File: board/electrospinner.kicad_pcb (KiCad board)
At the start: 2 copper layers, 40 parts, among them J1 12Vin, J2 Programmer, J3 MotorConnector, J4 TempSensor, J5 USB_B, SW1 ResetBTN, U1 TPS62147, U2 FT230XS, U3 MSP430G2553IPW20

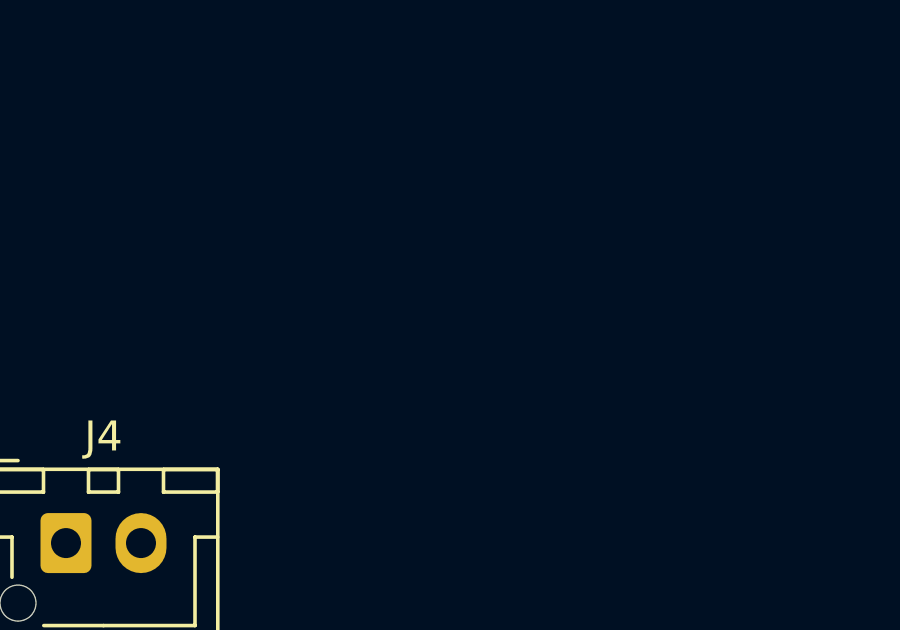
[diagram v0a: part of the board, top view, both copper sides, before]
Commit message: Updates schematic for rev6
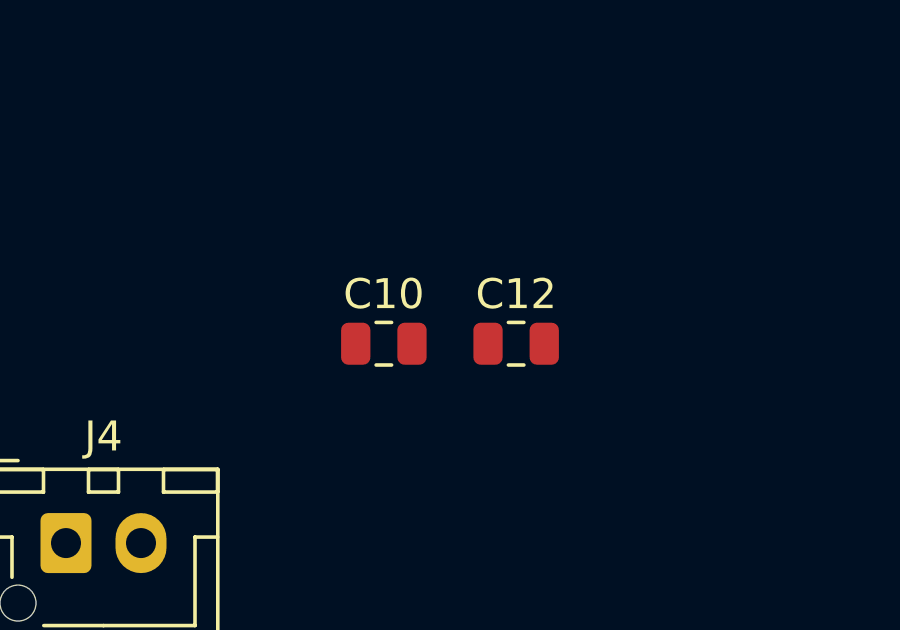
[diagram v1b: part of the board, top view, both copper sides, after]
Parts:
- added C10: 10uF, Capacitor_SMD:C_0805_2012Metric, F.Cu at (175.7, 68.3)
- added C12: 22uF, Capacitor_SMD:C_0805_2012Metric, F.Cu at (180.1, 68.3)
- J4: value TempSensor -> TempSensorConnector
- L1: value 1uH -> 2.2uH
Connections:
- R4 pad 1: /~RST -> +3V3
- R4 pad 2: GNDD -> /~RST
- SW1 pad 1: /~RST -> GNDD
- SW1 pad 2: +3V3 -> /~RST
- U1 pad 11: +12V -> GNDD
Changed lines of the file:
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@@
     (tracks 0)
     (zones 0)
-    (modules 40)
+    (modules 42)
     (nets 31)
   )
@@
     )
     (pad 11 smd rect (at -0.749998 -1.4) (size 0.249999 0.599999) (layers F.Paste)
-      (net 14 +12V))
+      (net 1 GNDD))
     (pad 11 smd rect (at -0.749998 -1.4) (size 0.249999 0.599999) (layers F.Mask)
-      (net 14 +12V))
+      (net 1 GNDD))
     (pad 11 smd rect (at -0.749998 -1.4) (size 0.249999 0.599999) (layers F.Cu)
-      (net 14 +12V))
+      (net 1 GNDD))
     (pad 10 smd rect (at -0.25 -1.4) (size 0.249999 0.599999) (layers F.Paste)
       (net 1 GNDD))
@@
     )
     (pad 1 thru_hole circle (at 6.5 0 90) (size 2 2) (drill 1.1) (layers *.Cu *.Mask)
+      (net 1 GNDD))
+    (pad 2 thru_hole circle (at 6.5 4.5 90) (size 2 2) (drill 1.1) (layers *.Cu *.Mask)
       (net 19 /~RST))
-    (pad 2 thru_hole circle (at 6.5 4.5 90) (size 2 2) (drill 1.1) (layers *.Cu *.Mask)
-      (net 17 +3V3))
     (pad 1 thru_hole circle (at 0 0 90) (size 2 2) (drill 1.1) (layers *.Cu *.Mask)
+      (net 1 GNDD))
+    (pad 2 thru_hole circle (at 0 4.5 90) (size 2 2) (drill 1.1) (layers *.Cu *.Mask)
       (net 19 /~RST))
-    (pad 2 thru_hole circle (at 0 4.5 90) (size 2 2) (drill 1.1) (layers *.Cu *.Mask)
-      (net 17 +3V3))
     (model ${KISYS3DMOD}/Button_Switch_THT.3dshapes/SW_PUSH_6mm_H5mm.wrl
       (at (xyz 0 0 0))
@@
     (fp_line (start -1 0.6) (end -1 -0.6) (layer F.Fab) (width 0.1))
     (pad 2 smd roundrect (at 0.9375 0) (size 0.975 1.4) (layers F.Cu F.Paste F.Mask) (roundrect_rratio 0.25)
-      (net 1 GNDD))
+      (net 19 /~RST))
     (pad 1 smd roundrect (at -0.9375 0) (size 0.975 1.4) (layers F.Cu F.Paste F.Mask) (roundrect_rratio 0.25)
-      (net 19 /~RST))
+      (net 17 +3V3))
     (model ${KISYS3DMOD}/Resistor_SMD.3dshapes/R_0805_2012Metric.wrl
       (at (xyz 0 0 0))
@@
       (effects (font (size 1 1) (thickness 0.15)))
     )
-    (fp_text value 1uH (at 0 1.65 270) (layer F.Fab)
+    (fp_text value 2.2uH (at 0 1.65 270) (layer F.Fab)
       (effects (font (size 1 1) (thickness 0.15)))
     )
@@
       (effects (font (size 1 1) (thickness 0.15)))
     )
-    (fp_text value TempSensor (at 1.25 4.6) (layer F.Fab)
+    (fp_text value TempSensorConnector (at 1.25 4.6) (layer F.Fab)
       (effects (font (size 1 1) (thickness 0.15)))
     )
@@
       (at (xyz 0 0 0))
       (scale (xyz 1 1 1))
+      (rotate (xyz 0 0 0))
+    )
+  )
+  (module Capacitor_SMD:C_0805_2012Metric (layer F.Cu)
+    (at 175.695001 68.285001)
+    (descr "Capacitor SMD 0805 (2012 Metric), square (rectangular) end terminal, IPC_7351 nominal, (Body size source: https://docs.google.com/spreadsheets/d/1BsfQQcO9C6DZCsRaXUlFlo91Tg2WpOkGARC1WS5S8t0/edit?usp=sharing), generated with kicad-footprint-generator")
+    (tags capacitor)
+    (attr smd)
+    (fp_text reference C10 (at 0 -1.65) (layer F.SilkS)
+      (effects (font (size 1 1) (thickness 0.15)))
+    )
+    (fp_text value 10uF (at 0 1.65) (layer F.Fab)
+      (effects (font (size 1 1) (thickness 0.15)))
+    )
+    (fp_text user %R (at 0 0) (layer F.Fab)
+      (effects (font (size 0.5 0.5) (thickness 0.08)))
+    )
+    (fp_line (start 1.68 0.95) (end -1.68 0.95) (layer F.CrtYd) (width 0.05))
+    (fp_line (start 1.68 -0.95) (end 1.68 0.95) (layer F.CrtYd) (width 0.05))
+    (fp_line (start -1.68 -0.95) (end 1.68 -0.95) (layer F.CrtYd) (width 0.05))
+    (fp_line (start -1.68 0.95) (end -1.68 -0.95) (layer F.CrtYd) (width 0.05))
+    (fp_line (start -0.258578 0.71) (end 0.258578 0.71) (layer F.SilkS) (width 0.12))
+    (fp_line (start -0.258578 -0.71) (end 0.258578 -0.71) (layer F.SilkS) (width 0.12))
+    (fp_line (start 1 0.6) (end -1 0.6) (layer F.Fab) (width 0.1))
+    (fp_line (start 1 -0.6) (end 1 0.6) (layer F.Fab) (width 0.1))
+    (fp_line (start -1 -0.6) (end 1 -0.6) (layer F.Fab) (width 0.1))
+    (fp_line (start -1 0.6) (end -1 -0.6) (layer F.Fab) (width 0.1))
+    (pad 2 smd roundrect (at 0.9375 0) (size 0.975 1.4) (layers F.Cu F.Paste F.Mask) (roundrect_rratio 0.25)
+      (net 1 GNDD))
+    (pad 1 smd roundrect (at -0.9375 0) (size 0.975 1.4) (layers F.Cu F.Paste F.Mask) (roundrect_rratio 0.25)
+      (net 17 +3V3))
+    (model ${KISYS3DMOD}/Capacitor_SMD.3dshapes/C_0805_2012Metric.wrl
+      (at (xyz 0 0 0))
+      (scale (xyz 1 1 1))
+      (rotate (xyz 0 0 0))
+    )
+  )
+  (module Capacitor_SMD:C_0805_2012Metric (layer F.Cu)
+    (at 180.105001 68.285001)
+    (descr "Capacitor SMD 0805 (2012 Metric), square (rectangular) end terminal, IPC_7351 nominal, (Body size source: https://docs.google.com/spreadsheets/d/1BsfQQcO9C6DZCsRaXUlFlo91Tg2WpOkGARC1WS5S8t0/edit?usp=sharing), generated with kicad-footprint-generator")
+    (tags capacitor)
+    (attr smd)
+    (fp_text reference C12 (at 0 -1.65) (layer F.SilkS)
+      (effects (font (size 1 1) (thickness 0.15)))
+    )
+    (fp_text value 22uF (at 0 1.65) (layer F.Fab)
+      (effects (font (size 1 1) (thickness 0.15)))
+    )
+    (fp_line (start -1 0.6) (end -1 -0.6) (layer F.Fab) (width 0.1))
+    (fp_line (start -1 -0.6) (end 1 -0.6) (layer F.Fab) (width 0.1))
+    (fp_line (start 1 -0.6) (end 1 0.6) (layer F.Fab) (width 0.1))
+    (fp_line (start 1 0.6) (end -1 0.6) (layer F.Fab) (width 0.1))
+    (fp_line (start -0.258578 -0.71) (end 0.258578 -0.71) (layer F.SilkS) (width 0.12))
+    (fp_line (start -0.258578 0.71) (end 0.258578 0.71) (layer F.SilkS) (width 0.12))
+    (fp_line (start -1.68 0.95) (end -1.68 -0.95) (layer F.CrtYd) (width 0.05))
+    (fp_line (start -1.68 -0.95) (end 1.68 -0.95) (layer F.CrtYd) (width 0.05))
+    (fp_line (start 1.68 -0.95) (end 1.68 0.95) (layer F.CrtYd) (width 0.05))
+    (fp_line (start 1.68 0.95) (end -1.68 0.95) (layer F.CrtYd) (width 0.05))
+    (fp_text user %R (at 0 0) (layer F.Fab)
+      (effects (font (size 0.5 0.5) (thickness 0.08)))
+    )
+    (pad 1 smd roundrect (at -0.9375 0) (size 0.975 1.4) (layers F.Cu F.Paste F.Mask) (roundrect_rratio 0.25)
+      (net 17 +3V3))
+    (pad 2 smd roundrect (at 0.9375 0) (size 0.975 1.4) (layers F.Cu F.Paste F.Mask) (roundrect_rratio 0.25)
+      (net 1 GNDD))
+    (model ${KISYS3DMOD}/Capacitor_SMD.3dshapes/C_0805_2012Metric.wrl
+      (at (xyz 0 0 0))
+      (scale (xyz 1 1 1))

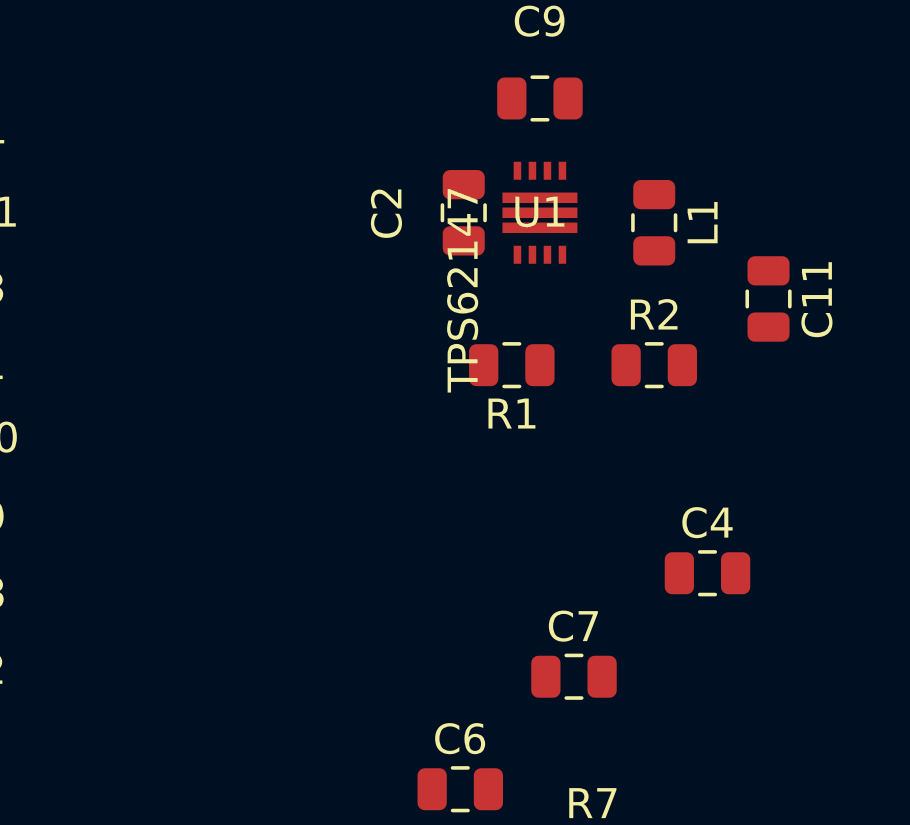
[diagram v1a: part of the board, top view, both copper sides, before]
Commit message: Updates the BOM and layout for rev6
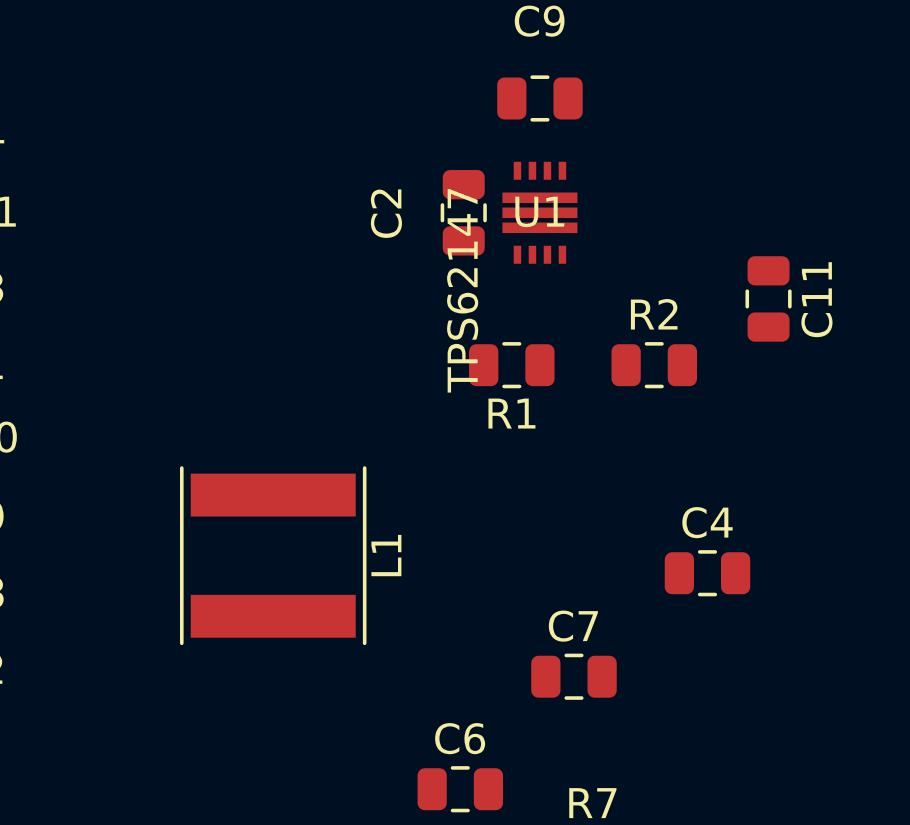
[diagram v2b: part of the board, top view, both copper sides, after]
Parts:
- L1: footprint Inductor_SMD:L_0805_2012Metric -> electrospinner:L_Coilcraft_XEL6030
- moved L1 16.9 mm to (174.0, 97.8)
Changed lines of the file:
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@@
-    )
-  )
-  (module Inductor_SMD:L_0805_2012Metric (layer F.Cu)
-    (at 186.69 86.6925 270)
-    (descr "Inductor SMD 0805 (2012 Metric), square (rectangular) end terminal, IPC_7351 nominal, (Body size source: https://docs.google.com/spreadsheets/d/1BsfQQcO9C6DZCsRaXUlFlo91Tg2WpOkGARC1WS5S8t0/edit?usp=sharing), generated with kicad-footprint-generator")
-    (tags inductor)
-    (attr smd)
-    (fp_text reference L1 (at 0 -1.65 270) (layer F.SilkS)
-      (effects (font (size 1 1) (thickness 0.15)))
-    )
-    (fp_text value 2.2uH (at 0 1.65 270) (layer F.Fab)
-      (effects (font (size 1 1) (thickness 0.15)))
-    )
-    (fp_text user %R (at 0 0 270) (layer F.Fab)
-      (effects (font (size 0.5 0.5) (thickness 0.08)))
-    )
-    (fp_line (start 1.68 0.95) (end -1.68 0.95) (layer F.CrtYd) (width 0.05))
-    (fp_line (start 1.68 -0.95) (end 1.68 0.95) (layer F.CrtYd) (width 0.05))
-    (fp_line (start -1.68 -0.95) (end 1.68 -0.95) (layer F.CrtYd) (width 0.05))
-    (fp_line (start -1.68 0.95) (end -1.68 -0.95) (layer F.CrtYd) (width 0.05))
-    (fp_line (start -0.258578 0.71) (end 0.258578 0.71) (layer F.SilkS) (width 0.12))
-    (fp_line (start -0.258578 -0.71) (end 0.258578 -0.71) (layer F.SilkS) (width 0.12))
-    (fp_line (start 1 0.6) (end -1 0.6) (layer F.Fab) (width 0.1))
-    (fp_line (start 1 -0.6) (end 1 0.6) (layer F.Fab) (width 0.1))
-    (fp_line (start -1 -0.6) (end 1 -0.6) (layer F.Fab) (width 0.1))
-    (fp_line (start -1 0.6) (end -1 -0.6) (layer F.Fab) (width 0.1))
-    (pad 2 smd roundrect (at 0.9375 0 270) (size 0.975 1.4) (layers F.Cu F.Paste F.Mask) (roundrect_rratio 0.25)
-      (net 17 +3V3))
-    (pad 1 smd roundrect (at -0.9375 0 270) (size 0.975 1.4) (layers F.Cu F.Paste F.Mask) (roundrect_rratio 0.25)
-      (net 23 "Net-(L1-Pad1)"))
-    (model ${KISYS3DMOD}/Inductor_SMD.3dshapes/L_0805_2012Metric.wrl
-      (at (xyz 0 0 0))
-      (scale (xyz 1 1 1))
-      (rotate (xyz 0 0 0))
     )
   )
@@
       (at (xyz 0 0 0))
       (scale (xyz 1 1 1))
+      (rotate (xyz 0 0 0))
+    )
+  )
+  (module electrospinner:L_Coilcraft_XEL6030 (layer F.Cu)
+    (at 173.99 97.79 270)
+    (descr L_Coilcraft_XAL5030)
+    (tags "L Coilcraft XAL5030")
+    (attr smd)
+    (fp_text reference L1 (at 0 -3.81 270) (layer F.SilkS)
+      (effects (font (size 1 1) (thickness 0.15)))
+    )
+    (fp_text value 2.2uH (at 0 4.572 270) (layer F.Fab)
+      (effects (font (size 1 1) (thickness 0.15)))
+    )
+    (fp_text user %R (at 0 0) (layer F.Fab)
+      (effects (font (size 0.75 0.75) (thickness 0.15)))
+    )
+    (fp_line (start 2.921 3.048) (end -2.921 3.048) (layer F.SilkS) (width 0.12))
+    (fp_line (start -2.921 -3.048) (end 2.921 -3.048) (layer F.SilkS) (width 0.12))
+    (fp_line (start -3.048 3.175) (end -3.048 -3.175) (layer F.CrtYd) (width 0.05))
+    (fp_line (start 3.048 3.175) (end -3.048 3.175) (layer F.CrtYd) (width 0.05))
+    (fp_line (start 3.048 -3.175) (end 3.048 3.175) (layer F.CrtYd) (width 0.05))
+    (fp_line (start -3.048 -3.175) (end 3.048 -3.175) (layer F.CrtYd) (width 0.05))
+    (fp_line (start -2.921 2.921) (end -2.921 -2.921) (layer F.Fab) (width 0.1))
+    (fp_line (start 2.921 2.921) (end -2.921 2.921) (layer F.Fab) (width 0.1))
+    (fp_line (start 2.921 -2.921) (end 2.921 2.921) (layer F.Fab) (width 0.1))
+    (fp_line (start -2.921 -2.921) (end 2.921 -2.921) (layer F.Fab) (width 0.1))
+    (pad 1 smd rect (at -2.02 0 270) (size 1.43 5.5) (layers F.Cu F.Paste F.Mask)
+      (net 23 "Net-(L1-Pad1)"))
+    (pad 2 smd rect (at 2.02 0 270) (size 1.43 5.5) (layers F.Cu F.Paste F.Mask)
+      (net 17 +3V3))
+    (model ${KISYS3DMOD}/Inductor_SMD.3dshapes/L_Coilcraft_XAL5030.wrl
+      (at (xyz 0 0 0))
+      (scale (xyz 1 1 1))
